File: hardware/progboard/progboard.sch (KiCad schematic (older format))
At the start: 23 parts, among them J1 LEFT, J2 RIGHT, J3 SWD, J4 CV A, J5 POWER

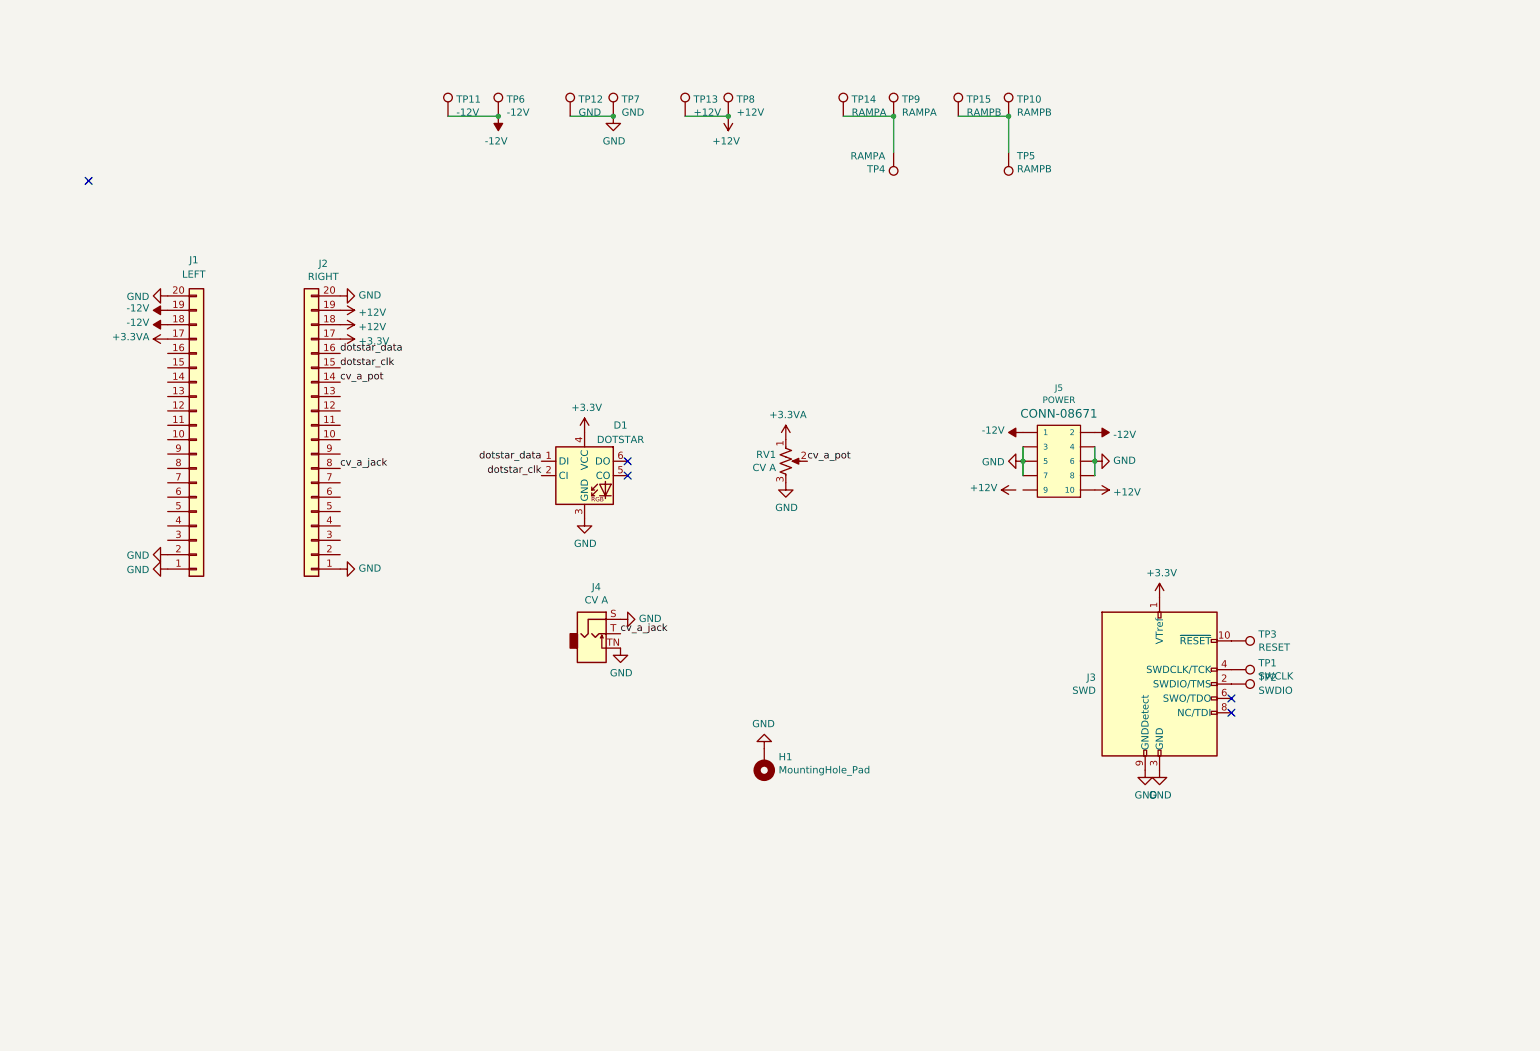
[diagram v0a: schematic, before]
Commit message: Add LEDs to the progboard
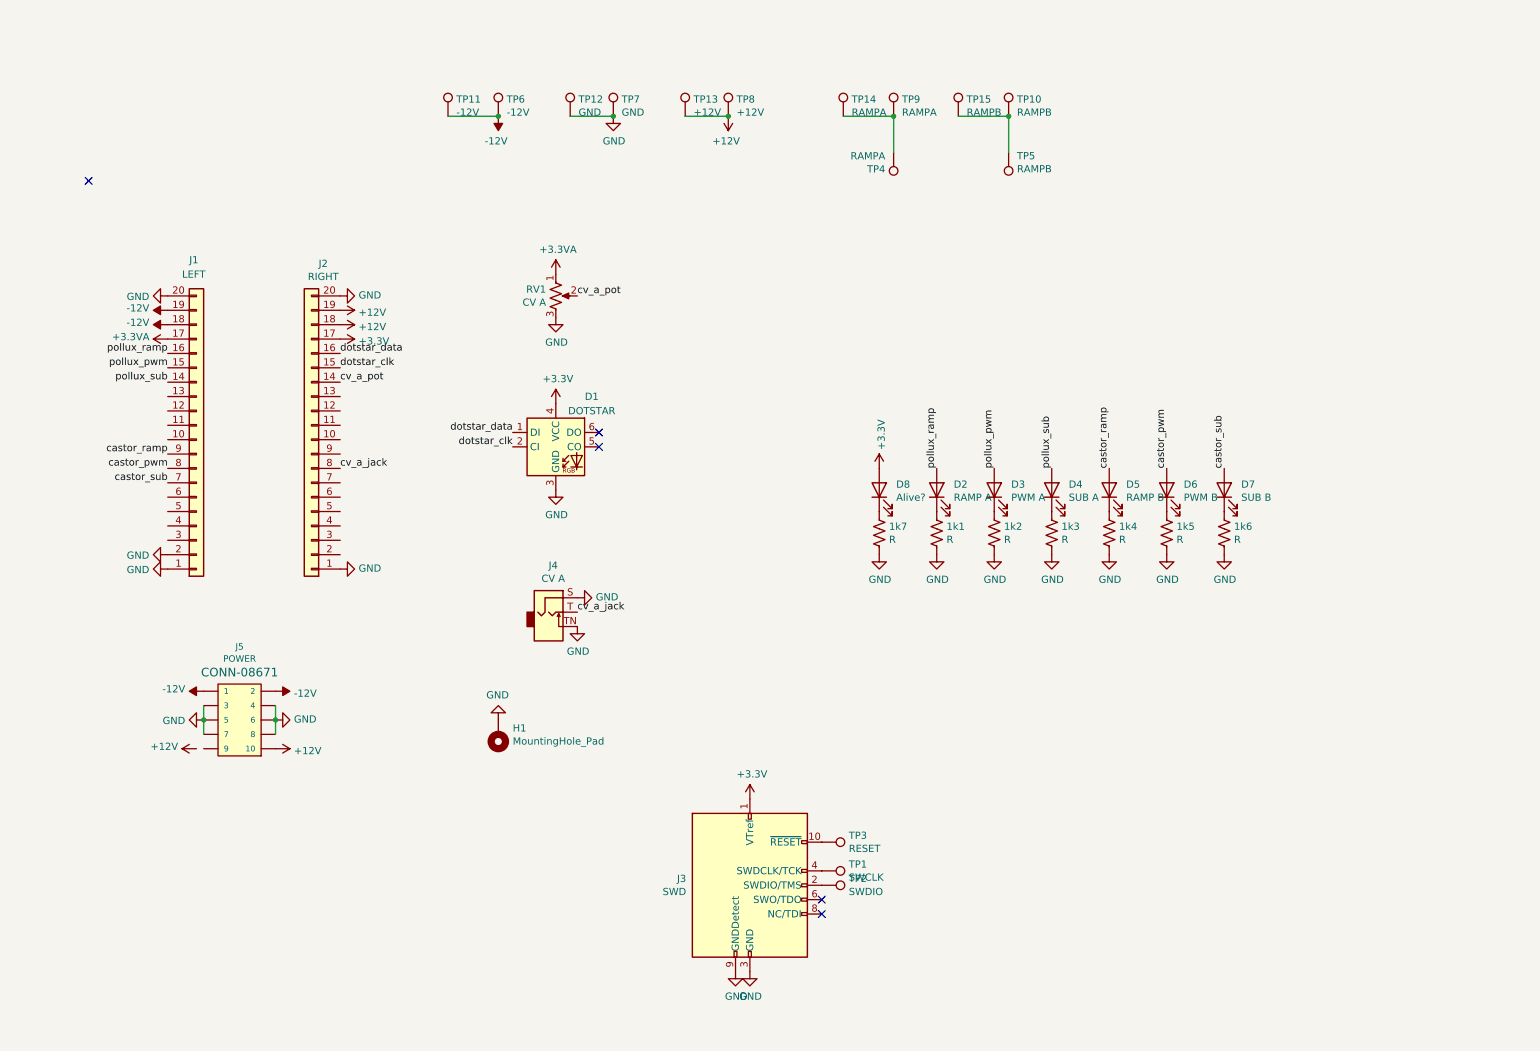
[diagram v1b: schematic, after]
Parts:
- added 1k1, 1k2, 1k3, 1k4, 1k5, 1k6, 1k7: R, Resistor_THT:R_Axial_DIN0207_L6.3mm_D2.5mm_P7.62mm_Horizontal, symbol Device:R_US
- added D2: RAMP A, LED_THT:LED_D5.0mm, symbol Device:LED
- added D3: PWM A, LED_THT:LED_D5.0mm, symbol Device:LED
- added D4: SUB A, LED_THT:LED_D5.0mm, symbol Device:LED
- added D5: RAMP B, LED_THT:LED_D5.0mm, symbol Device:LED
- added D6: PWM B, LED_THT:LED_D5.0mm, symbol Device:LED
- added D7: SUB B, LED_THT:LED_D5.0mm, symbol Device:LED
- added D8: Alive?, LED_THT:LED_D5.0mm, symbol Device:LED
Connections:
- net +3V3: now also D8.2 (A)
- net GND: now also 1k1.2, 1k2.2, 1k3.2, 1k4.2, 1k5.2, 1k6.2, 1k7.2
- net pollux_sub: now reaches J1.14 (Pin_14)
- net pollux_sub: now also D4.2 (A)
- net pollux_pwm: now reaches J1.15 (Pin_15)
- net pollux_pwm: now also D3.2 (A)
- net pollux_ramp: now reaches J1.16 (Pin_16)
- net pollux_ramp: now also D2.2 (A)
- net castor_sub: now reaches J1.7 (Pin_7)
- net castor_sub: now also D7.2 (A)
- net castor_pwm: now reaches J1.8 (Pin_8)
- net castor_pwm: now also D6.2 (A)
- net castor_ramp: now reaches J1.9 (Pin_9)
- net castor_ramp: now also D5.2 (A)
- new net: 1k1.1, D2.1 (K)
- new net: 1k2.1, D3.1 (K)
- new net: 1k3.1, D4.1 (K)
- new net: 1k4.1, D5.1 (K)
- new net: 1k5.1, D6.1 (K)
- new net: 1k6.1, D7.1 (K)
- new net: 1k7.1, D8.1 (K)
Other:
- moved on the sheet: D1, H1, J3, J4, J5, RV1, TP1, TP2, TP3

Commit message: Adjust drill sizes for pogo pins
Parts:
- TP1, TP2, TP3, TP4, TP5: footprint TestPoint:TestPoint_THTPad_D1.0mm_Drill0.5mm -> TestPoint:TestPoint_THTPad_D1.5mm_Drill0.7mm
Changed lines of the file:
@@
 F 0 "TP1" V 6104 6788 50  0000 L CNN
 F 1 "SWCLK" V 6195 6788 50  0000 L CNN
-F 2 "TestPoint:TestPoint_THTPad_D1.0mm_Drill0.5mm" H 6350 6600 50  0001 C CNN
+F 2 "TestPoint:TestPoint_THTPad_D1.5mm_Drill0.7mm" H 6350 6600 50  0001 C CNN
 F 3 "~" H 6350 6600 50  0001 C CNN
 	1    6150 6600
@@
 F 0 "TP2" V 6104 6888 50  0000 L CNN
 F 1 "SWDIO" V 6195 6888 50  0000 L CNN
-F 2 "TestPoint:TestPoint_THTPad_D1.0mm_Drill0.5mm" H 6350 6700 50  0001 C CNN
+F 2 "TestPoint:TestPoint_THTPad_D1.5mm_Drill0.7mm" H 6350 6700 50  0001 C CNN
 F 3 "~" H 6350 6700 50  0001 C CNN
 	1    6150 6700
@@
 F 0 "TP3" V 6104 6588 50  0000 L CNN
 F 1 "RESET" V 6195 6588 50  0000 L CNN
-F 2 "TestPoint:TestPoint_THTPad_D1.0mm_Drill0.5mm" H 6350 6400 50  0001 C CNN
+F 2 "TestPoint:TestPoint_THTPad_D1.5mm_Drill0.7mm" H 6350 6400 50  0001 C CNN
 F 3 "~" H 6350 6400 50  0001 C CNN
 	1    6150 6400
@@
 F 0 "TP4" H 6708 1718 50  0000 L CNN
 F 1 "RAMPA" H 6708 1627 50  0000 L CNN
-F 2 "TestPoint:TestPoint_THTPad_D1.0mm_Drill0.5mm" H 6850 1600 50  0001 C CNN
+F 2 "TestPoint:TestPoint_THTPad_D1.5mm_Drill0.7mm" H 6850 1600 50  0001 C CNN
 F 3 "~" H 6850 1600 50  0001 C CNN
 	1    6650 1600
@@
 F 0 "TP5" H 7392 1626 50  0000 R CNN
 F 1 "RAMPB" H 7392 1717 50  0000 R CNN
-F 2 "TestPoint:TestPoint_THTPad_D1.0mm_Drill0.5mm" H 7650 1600 50  0001 C CNN
+F 2 "TestPoint:TestPoint_THTPad_D1.5mm_Drill0.7mm" H 7650 1600 50  0001 C CNN
 F 3 "~" H 7650 1600 50  0001 C CNN
 	1    7450 1600

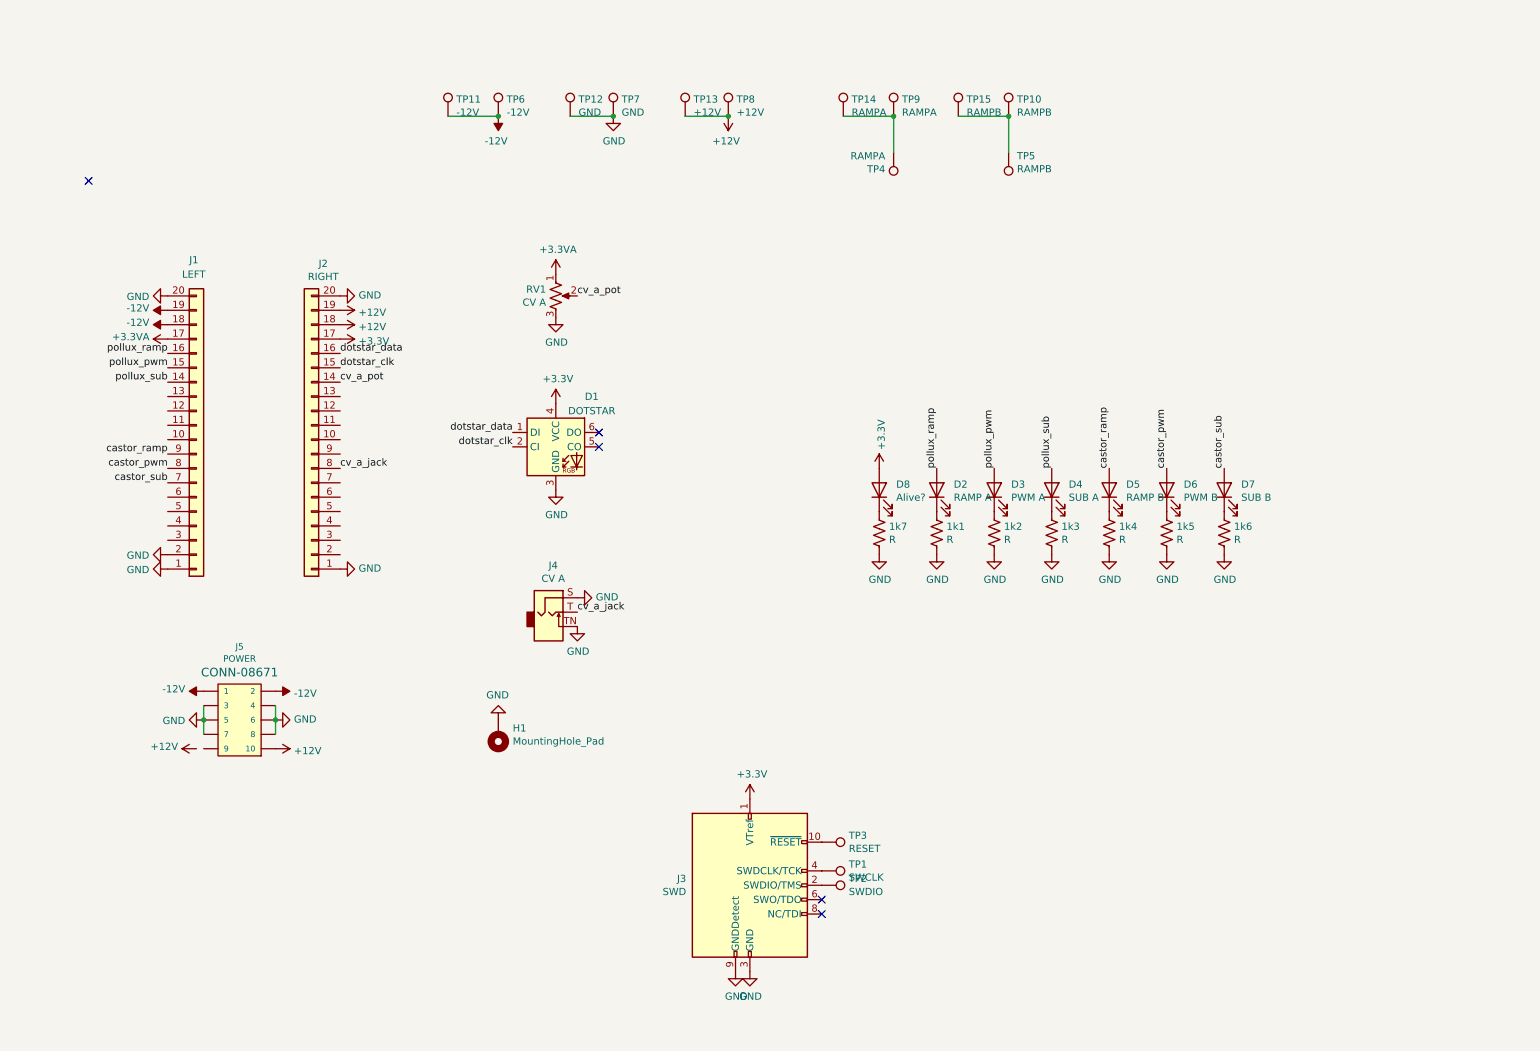
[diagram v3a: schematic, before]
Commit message: hardware: new revision of programming board with more comprehensive test points
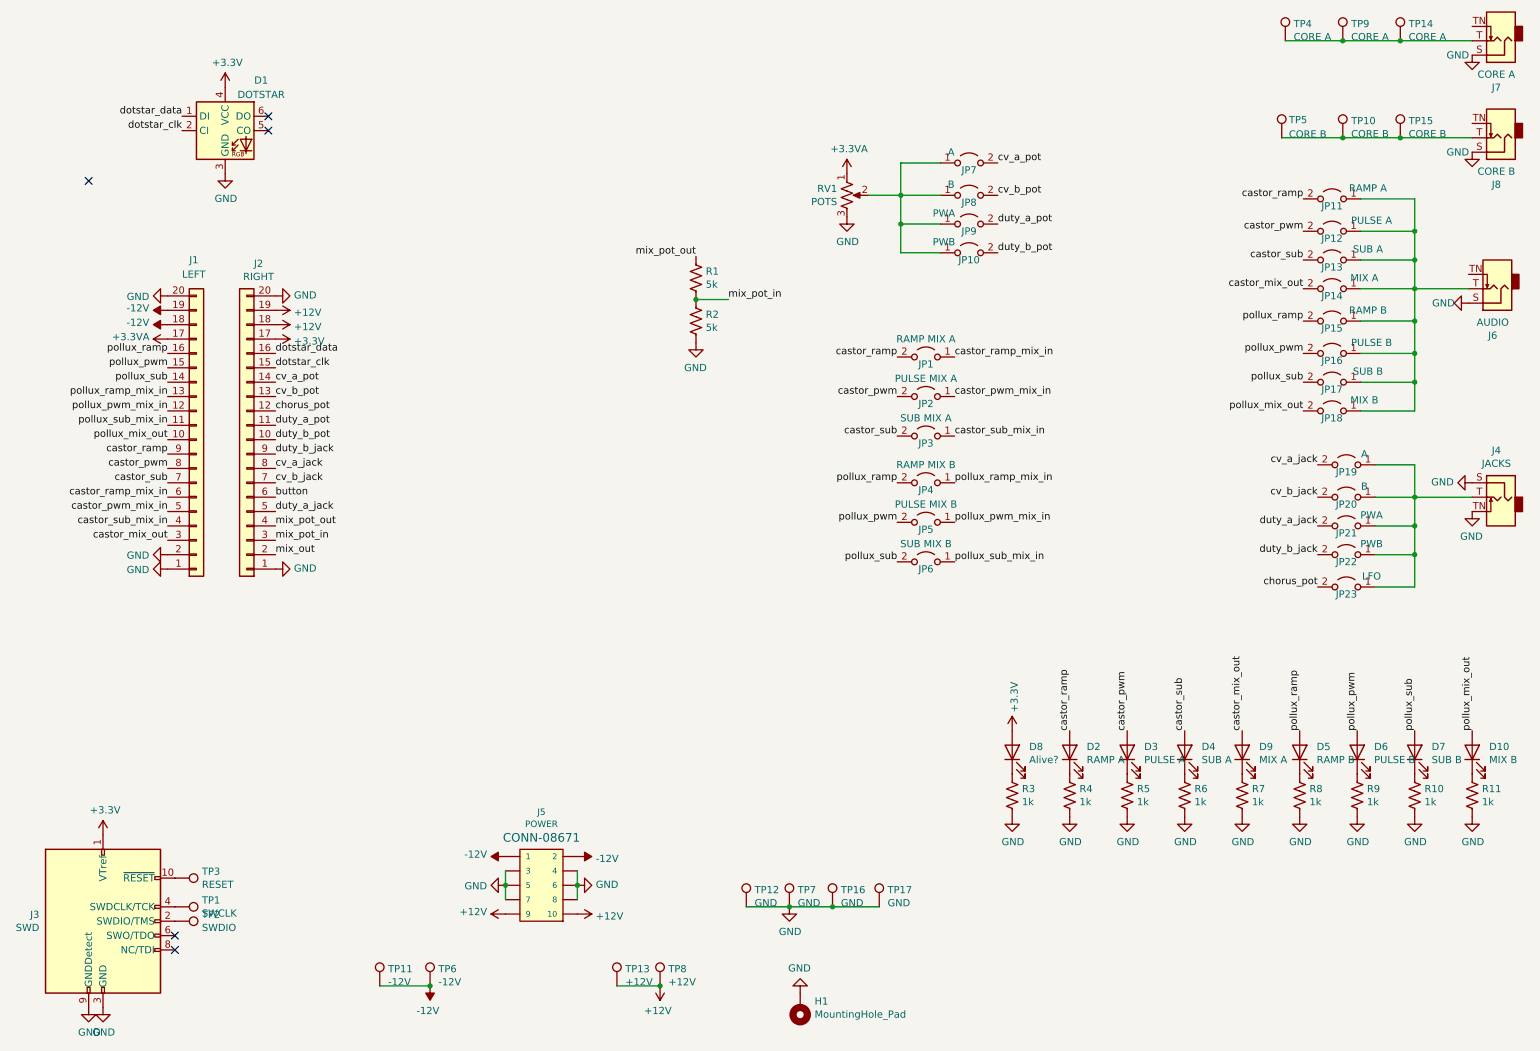
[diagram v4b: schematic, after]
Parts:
- added D10: MIX B, LED_THT:LED_D5.0mm, symbol Device:LED
- added D9: MIX A, LED_THT:LED_D5.0mm, symbol Device:LED
- added J6: AUDIO, progboard:WQP-PJ301M-12_JACK, symbol Connector:AudioJack2_SwitchT
- added J7: CORE A, progboard:WQP-PJ301M-12_JACK, symbol Connector:AudioJack2_SwitchT
- added J8: CORE B, progboard:WQP-PJ301M-12_JACK, symbol Connector:AudioJack2_SwitchT
- added JP1: RAMP MIX A, TestPoint:TestPoint_2Pads_Pitch2.54mm_Drill0.8mm, symbol Jumper:Jumper_2_Open
- added JP10, JP22: PWB, TestPoint:TestPoint_2Pads_Pitch2.54mm_Drill0.8mm, symbol Jumper:Jumper_2_Open
- added JP11: RAMP A, TestPoint:TestPoint_2Pads_Pitch2.54mm_Drill0.8mm, symbol Jumper:Jumper_2_Open
- added JP12: PULSE A, TestPoint:TestPoint_2Pads_Pitch2.54mm_Drill0.8mm, symbol Jumper:Jumper_2_Open
- added JP13: SUB A, TestPoint:TestPoint_2Pads_Pitch2.54mm_Drill0.8mm, symbol Jumper:Jumper_2_Open
- added JP14: MIX A, TestPoint:TestPoint_2Pads_Pitch2.54mm_Drill0.8mm, symbol Jumper:Jumper_2_Open
- added JP15: RAMP B, TestPoint:TestPoint_2Pads_Pitch2.54mm_Drill0.8mm, symbol Jumper:Jumper_2_Open
- added JP16: PULSE B, TestPoint:TestPoint_2Pads_Pitch2.54mm_Drill0.8mm, symbol Jumper:Jumper_2_Open
- added JP17: SUB B, TestPoint:TestPoint_2Pads_Pitch2.54mm_Drill0.8mm, symbol Jumper:Jumper_2_Open
- added JP18: MIX B, TestPoint:TestPoint_2Pads_Pitch2.54mm_Drill0.8mm, symbol Jumper:Jumper_2_Open
- added JP19, JP7: A, TestPoint:TestPoint_2Pads_Pitch2.54mm_Drill0.8mm, symbol Jumper:Jumper_2_Open
- added JP2: PULSE MIX A, TestPoint:TestPoint_2Pads_Pitch2.54mm_Drill0.8mm, symbol Jumper:Jumper_2_Open
- added JP20, JP8: B, TestPoint:TestPoint_2Pads_Pitch2.54mm_Drill0.8mm, symbol Jumper:Jumper_2_Open
- added JP21, JP9: PWA, TestPoint:TestPoint_2Pads_Pitch2.54mm_Drill0.8mm, symbol Jumper:Jumper_2_Open
- added JP23: LFO, TestPoint:TestPoint_2Pads_Pitch2.54mm_Drill0.8mm, symbol Jumper:Jumper_2_Open
- added JP3: SUB MIX A, TestPoint:TestPoint_2Pads_Pitch2.54mm_Drill0.8mm, symbol Jumper:Jumper_2_Open
- added JP4: RAMP MIX B, TestPoint:TestPoint_2Pads_Pitch2.54mm_Drill0.8mm, symbol Jumper:Jumper_2_Open
- added JP5: PULSE MIX B, TestPoint:TestPoint_2Pads_Pitch2.54mm_Drill0.8mm, symbol Jumper:Jumper_2_Open
- added JP6: SUB MIX B, TestPoint:TestPoint_2Pads_Pitch2.54mm_Drill0.8mm, symbol Jumper:Jumper_2_Open
- added R1, R2: 5k, Resistor_THT:R_Axial_DIN0207_L6.3mm_D2.5mm_P7.62mm_Horizontal, symbol Device:R_US
- added R11, R7: 1k, Resistor_THT:R_Axial_DIN0207_L6.3mm_D2.5mm_P7.62mm_Horizontal, symbol Device:R_US
- added TP16, TP17: GND, TestPoint:TestPoint_Plated_Hole_D3.0mm, symbol Connector:TestPoint
- D3: value PWM A -> PULSE A
- D6: value PWM B -> PULSE B
- J4: value CV A -> JACKS
- R10: renamed from 1k6; value R -> 1k
- R3: renamed from 1k7; value R -> 1k
- R4: renamed from 1k1; value R -> 1k
- R5: renamed from 1k2; value R -> 1k
- R6: renamed from 1k3; value R -> 1k
- R8: renamed from 1k4; value R -> 1k
- R9: renamed from 1k5; value R -> 1k
- RV1: value CV A -> POTS
- TP10, TP15, TP5: value RAMPB -> CORE B
- TP14, TP4, TP9: value RAMPA -> CORE A
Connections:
- net +12V: now also J5.9
- net GND: now also J6.S, J7.S, J8.S, R11.2, R2.2, R7.2, TP16.1, TP17.1
- net castor_pwm: now also D3.2 (A), JP12.2 (B), JP2.2 (B); no longer D6.2 (A)
- net castor_ramp: now also D2.2 (A), JP1.2 (B), JP11.2 (B); no longer D5.2 (A)
- net castor_sub: now also D4.2 (A), JP13.2 (B), JP3.2 (B); no longer D7.2 (A)
- net cv_a_jack: now also JP19.2 (B); no longer J4.T
- net cv_a_pot: now also JP7.2 (B); no longer RV1.2
- net pollux_pwm: now also D6.2 (A), JP16.2 (B), JP5.2 (B); no longer D3.2 (A)
- net pollux_ramp: now also D5.2 (A), JP15.2 (B), JP4.2 (B); no longer D2.2 (A)
- net pollux_sub: now also D7.2 (A), JP17.2 (B), JP6.2 (B); no longer D4.2 (A)
- net pollux_mix_out: now reaches J1.10 (Pin_10)
- net pollux_mix_out: now also D10.2 (A), JP18.2 (B)
- net pollux_sub_mix_in: now reaches J1.11 (Pin_11)
- net pollux_sub_mix_in: now also JP6.1 (A)
- net pollux_pwm_mix_in: now reaches J1.12 (Pin_12)
- net pollux_pwm_mix_in: now also JP5.1 (A)
- net pollux_ramp_mix_in: now reaches J1.13 (Pin_13)
- net pollux_ramp_mix_in: now also JP4.1 (A)
- net castor_mix_out: now reaches J1.3 (Pin_3)
- net castor_mix_out: now also D9.2 (A), JP14.2 (B)
- net castor_sub_mix_in: now reaches J1.4 (Pin_4)
- net castor_sub_mix_in: now also JP3.1 (A)
- net castor_pwm_mix_in: now reaches J1.5 (Pin_5)
- net castor_pwm_mix_in: now also JP2.1 (A)
- net castor_ramp_mix_in: now reaches J1.6 (Pin_6)
- net castor_ramp_mix_in: now also JP1.1 (A)
- net duty_b_pot: now reaches J2.10 (Pin_10)
- net duty_b_pot: now also JP10.2 (B)
- net duty_a_pot: now reaches J2.11 (Pin_11)
- net duty_a_pot: now also JP9.2 (B)
- net chorus_pot: now reaches J2.12 (Pin_12)
- net chorus_pot: now also JP23.2 (B)
- net cv_b_pot: now reaches J2.13 (Pin_13)
- net cv_b_pot: now also JP8.2 (B)
- net mix_out: now reaches J2.2 (Pin_2)
- net mix_pot_in: now reaches J2.3 (Pin_3)
- net mix_pot_in: now also R1.2, R2.1
- net mix_pot_out: now reaches J2.4 (Pin_4)
- net mix_pot_out: now also R1.1
- net duty_a_jack: now reaches J2.5 (Pin_5)
- net duty_a_jack: now also JP21.2 (B)
- net button: now reaches J2.6 (Pin_6)
- net cv_b_jack: now reaches J2.7 (Pin_7)
- net cv_b_jack: now also JP20.2 (B)
- net duty_b_jack: now reaches J2.9 (Pin_9)
- net duty_b_jack: now also JP22.2 (B)
- net at TP14.1, TP4.1, TP9.1: now also J7.T
- net at TP10.1, TP15.1, TP5.1: now also J8.T
- new net: JP10.1 (A), JP7.1 (A), JP8.1 (A), JP9.1 (A), RV1.2
- new net: J4.T, JP19.1 (A), JP20.1 (A), JP21.1 (A), JP22.1 (A), JP23.1 (A)
- new net: J6.T, JP11.1 (A), JP12.1 (A), JP13.1 (A), JP14.1 (A), JP15.1 (A), JP16.1 (A), JP17.1 (A), JP18.1 (A)
- new net: D9.1 (K), R7.1
- new net: D10.1 (K), R11.1
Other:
- moved on the sheet: D1, D2, D3, D4, D5, D6, D7, D8, H1, J2, J3, J4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
